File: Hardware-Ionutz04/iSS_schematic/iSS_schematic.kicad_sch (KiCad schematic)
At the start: 12 parts, among them J1 Conn_02x04_Row_Letter_First, J2 Screw_Terminal_01x02, J3 Screw_Terminal_01x02, U1 ACS37800KMACTR-030B3-I2C

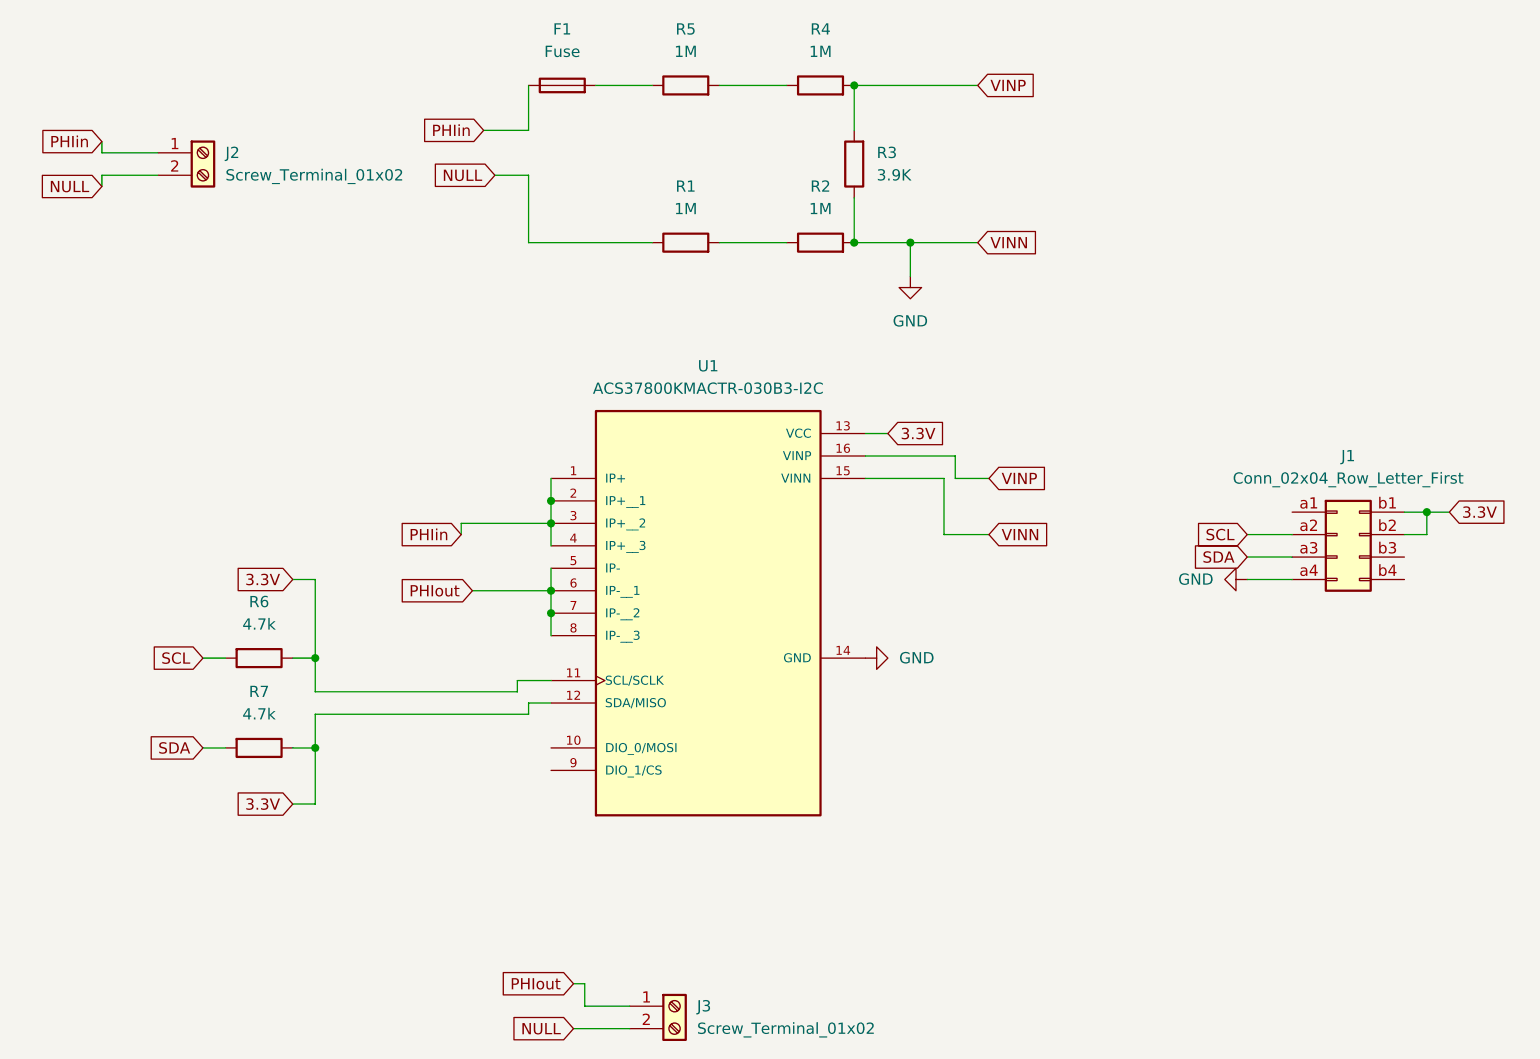
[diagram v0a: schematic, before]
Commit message: Revert "Beta commit on firmware side of the iSS"
This reverts commit 418c5d5a18d21a18faee41e17dfe4be9b8e227ae.
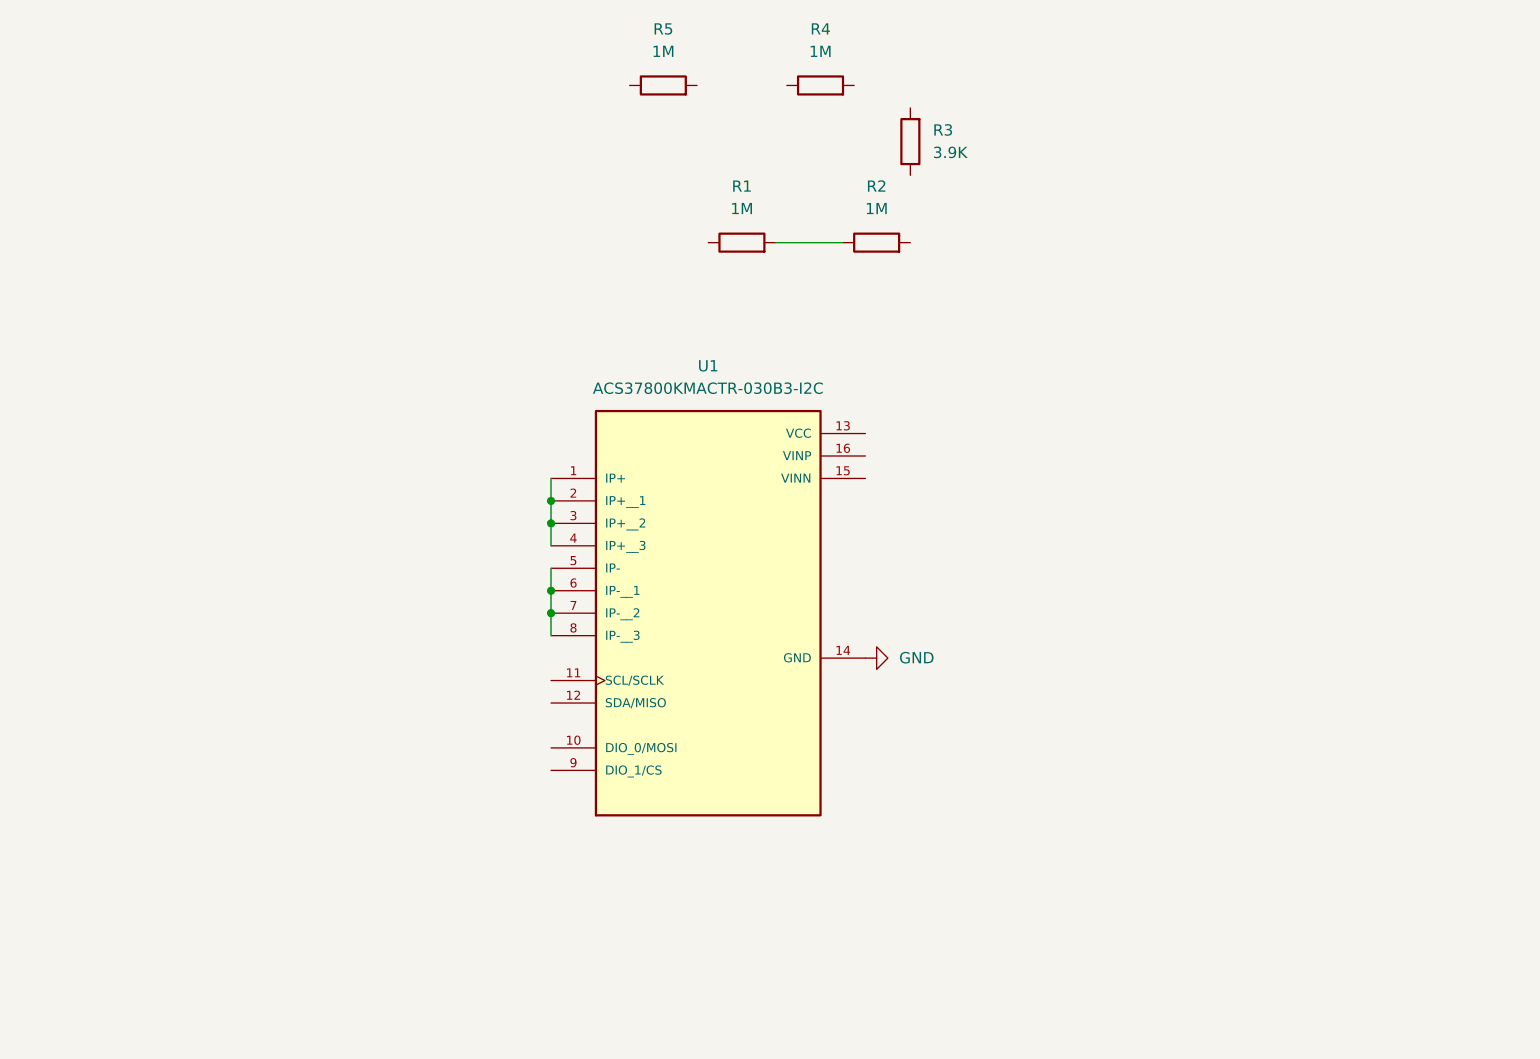
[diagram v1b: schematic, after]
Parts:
- removed F1: Fuse, Fuse:Fuse_0603_1608Metric_Pad1.05x0.95mm_HandSolder, symbol Device:Fuse
- removed J1: Conn_02x04_Row_Letter_First, Connector_PinHeader_2.54mm:PinHeader_2x04_P2.54mm_Vertical, symbol Connector_Generic:Conn_02x04_Row_Letter_First
- removed J2, J3: Screw_Terminal_01x02, TerminalBlock_CUI:TerminalBlock_CUI_TB007-508-02_1x02_P5.08mm_Horizontal, symbol Connector:Screw_Terminal_01x02
- removed R6, R7: 4.7k, Resistor_SMD:R_1206_3216Metric_Pad1.30x1.75mm_HandSolder, symbol Device:R
- R1, R2, R3, R4, R5: footprint Resistor_SMD:R_1206_3216Metric_Pad1.30x1.75mm_HandSolder -> (none)
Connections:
- net GND: no longer R2.2, R3.1, U1.15 (VINN)
- net at R4.1: no longer R5.2
- removed net 3.3V: U1.11 (SCL/SCLK), U1.12 (SDA/MISO), U1.13 (VCC)
- net NULL: no longer names the net of R1.1
- net PHIin: no longer names the net of U1.1 (IP+), U1.2 (IP+__1), U1.3 (IP+__2), U1.4 (IP+__3)
- net PHIout: no longer names the net of U1.5 (IP-), U1.6 (IP-__1), U1.7 (IP-__2), U1.8 (IP-__3)
- removed net VINP: R3.2, R4.2, U1.16 (VINP)
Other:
- moved on the sheet: R1, R2, R3, R5

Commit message: Beta commit on firmware side of the iSS
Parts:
- added F1: Fuse, Fuse:Fuse_0603_1608Metric_Pad1.05x0.95mm_HandSolder, symbol Device:Fuse
- added J1: Conn_02x04_Row_Letter_First, Connector_PinHeader_2.54mm:PinHeader_2x04_P2.54mm_Vertical, symbol Connector_Generic:Conn_02x04_Row_Letter_First
- added J2, J3: Screw_Terminal_01x02, TerminalBlock_CUI:TerminalBlock_CUI_TB007-508-02_1x02_P5.08mm_Horizontal, symbol Connector:Screw_Terminal_01x02
- added R6, R7: 4.7k, Resistor_SMD:R_1206_3216Metric_Pad1.30x1.75mm_HandSolder, symbol Device:R
- R1, R2, R3, R4, R5: footprint (none) -> Resistor_SMD:R_1206_3216Metric_Pad1.30x1.75mm_HandSolder
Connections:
- net GND: now also R2.2, R3.1, U1.15 (VINN), J1.a4 (Pin_a4)
- net NULL: now reaches R1.1
- net NULL: now also J2.2 (Pin_2), J3.2 (Pin_2)
- net PHIin: now reaches U1.1 (IP+), U1.2 (IP+__1), U1.3 (IP+__2), U1.4 (IP+__3)
- net PHIin: now also F1.1, J2.1 (Pin_1)
- net 3.3V: now reaches U1.11 (SCL/SCLK)
- net 3.3V: now also U1.12 (SDA/MISO), U1.13 (VCC), J1.b1 (Pin_b1), J1.b2 (Pin_b2), R6.1, R7.1
- net VINP: now reaches U1.16 (VINP)
- net VINP: now also R3.2, R4.2
- net PHIout: now reaches U1.5 (IP-), U1.6 (IP-__1), U1.7 (IP-__2), U1.8 (IP-__3)
- net PHIout: now also J3.1 (Pin_1)
- net at R4.1: now also R5.2
- net at R5.1: now also F1.2
- new net SCL: J1.a2 (Pin_a2), R6.2
- new net SDA: J1.a3 (Pin_a3), R7.2
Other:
- moved on the sheet: R1, R2, R3, R5
